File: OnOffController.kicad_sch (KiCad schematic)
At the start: 10 parts, among them J1 USB_B_Micro, U1 STM6601, U2 MCP73831-2-OT, U3 SPX3819M5-L

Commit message: Finished schematic
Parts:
- added C2, C3: 10uF, Capacitor_SMD:C_1206_3216Metric_Pad1.33x1.80mm_HandSolder, symbol Device:C
- added C4, C5: 1uF, Capacitor_SMD:C_1206_3216Metric_Pad1.33x1.80mm_HandSolder, symbol Device:C
- added C6: .33uF, Capacitor_SMD:C_1206_3216Metric_Pad1.33x1.80mm_HandSolder, symbol Device:C
- added C7: .1uF, Capacitor_SMD:C_1206_3216Metric_Pad1.33x1.80mm_HandSolder, symbol Device:C
- added D2: MBR0520, Diode_SMD:D_SOD-123, symbol Diode:MBR0520
- added D3: LED, LED_SMD:LED_1206_3216Metric_Pad1.42x1.75mm_HandSolder, symbol Device:LED
- added J2, J5: Conn_01x02_Pin, symbol Connector:Conn_01x02_Pin
- added J3, J4: Conn_01x04_Pin, symbol Connector:Conn_01x04_Pin
- added J6, J7: Conn_01x03_Pin, symbol Connector:Conn_01x03_Pin
- added R10, R5, R6, R7: 10K, Resistor_SMD:R_1206_3216Metric_Pad1.30x1.75mm_HandSolder, symbol Device:R
- added R8: 3.48K, Resistor_SMD:R_1206_3216Metric_Pad1.30x1.75mm_HandSolder, symbol Device:R
- added R9: 1K, Resistor_SMD:R_1206_3216Metric_Pad1.30x1.75mm_HandSolder, symbol Device:R
- added SW1: 2-1437565-8, 2-1437565-8:SW_SMD_2-1437565-8_4_4.50_6.00_6.00_5.00, symbol 2-1437565-8_CustomSwitch:2-1437565-8
- added TP1, TP2, TP3, TP4, TP5: TestPoint, symbol Connector:TestPoint
- C1: footprint (none) -> Capacitor_SMD:C_1206_3216Metric_Pad1.33x1.80mm_HandSolder
- D1: footprint (none) -> LED_SMD:LED_1206_3216Metric_Pad1.42x1.75mm_HandSolder
- R1, R2, R3, R4: footprint (none) -> Resistor_SMD:R_1206_3216Metric_Pad1.30x1.75mm_HandSolder
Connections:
- net GND: now also U1.12 (GND), U3.2 (GND), C2.2, C3.2, C4.2, C5.2, C6.2, C7.2, J2.2 (Pin_2), J4.4 (Pin_4), J7.1 (Pin_1), J7.2 (Pin_2), J7.3 (Pin_3), R10.2, SW1.1, SW1.2, TP2.1
- net VBUS: now also U1.1 (Vcc), U3.1 (IN), C2.1, C7.1, D2.1 (K), R9.1, TP3.1, TP4.1
- net VDC: now also D2.2 (A), TP5.1
- net EN_DIV: now reaches U3.3 (EN)
- net EN_DIV: now also J3.4 (Pin_4), R10.1, R8.2
- net +3V3: now reaches U3.5 (OUT)
- net +3V3: now also C3.1, C4.1, J3.1 (Pin_1), J5.1 (Pin_1), J6.1 (Pin_1), J6.2 (Pin_2), J6.3 (Pin_3), R5.1, R6.1, R7.1, TP1.1
- net BAT_SENSE: now reaches R3.2, R4.1
- net BAT_SENSE: now also J4.3 (Pin_3)
- net RST: now reaches U1.10 (~{RST})
- net RST: now also J3.3 (Pin_3), R6.2
- net INT: now reaches U1.11 (~{INT})
- net INT: now also J3.2 (Pin_2), R7.2
- net at U1.2 (~{SR}): now also U1.6 (~{PB}), J2.1 (Pin_1), SW1.3, SW1.4
- net Vref: now reaches U1.3 (Vref)
- net Vref: now also C5.1
- net PS_HOLD: now reaches U1.4 (PS_HOLD)
- net PS_HOLD: now also J4.2 (Pin_2), J5.2 (Pin_2)
- net at U1.5 (C_SRD): now also C6.1
- net at U1.7 (~{VCC}_LO): now also D3.1 (K)
- net PB_OUT: now reaches U1.8 (~{PB}_OUT)
- net PB_OUT: now also J4.1 (Pin_1), R5.2
- net EN: now reaches U1.9 (~{EN}/EN)
- net EN: now also R8.1
- new net: D3.2 (A), R9.2
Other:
- moved on the sheet: C1, D1, J1, R1, R2, R3, R4, U1, U2, U3

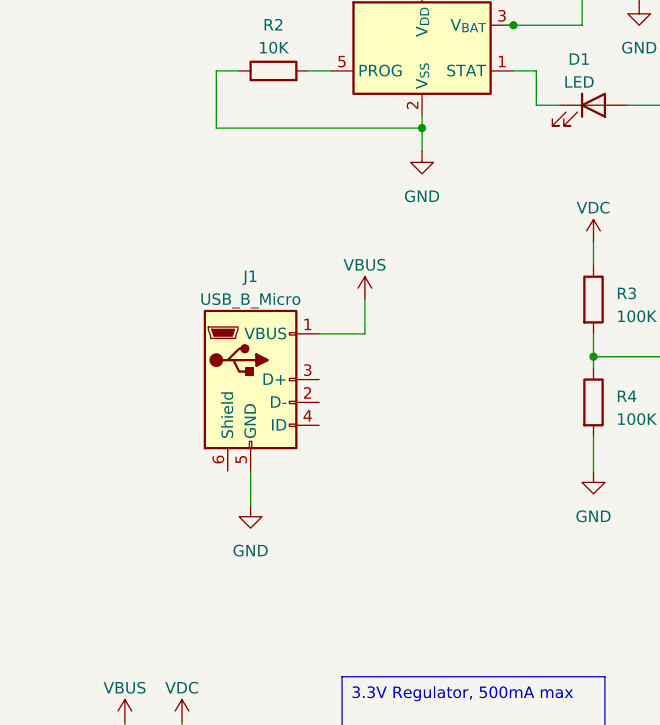
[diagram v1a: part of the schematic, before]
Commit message: Updated USB-B and switch footprints
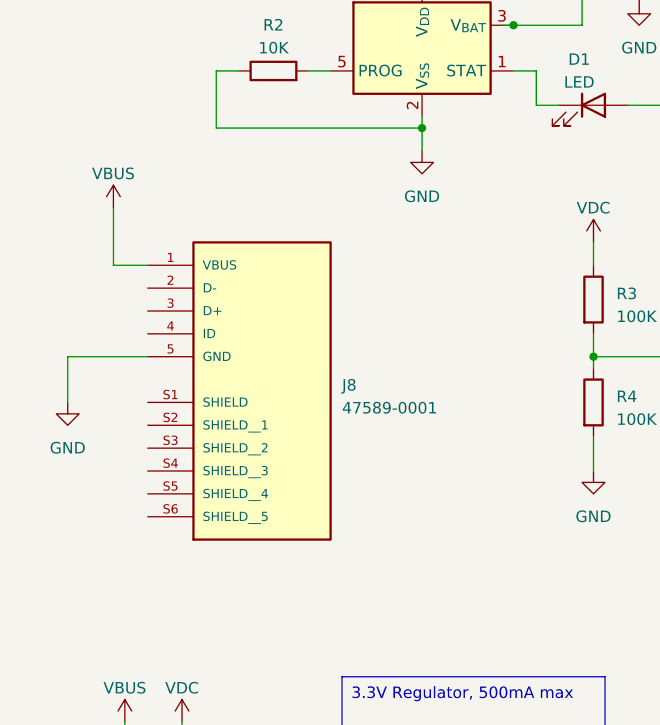
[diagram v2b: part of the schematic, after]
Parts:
- removed J1: USB_B_Micro, symbol Connector:USB_B_Micro
- added J8: 47589-0001, 47589_0001_USB_B:MOLEX_47589-0001, symbol 47589-0001_MOLEX_USB_B:47589-0001
- SW1: footprint 2-1437565-8:SW_SMD_2-1437565-8_4_4.50_6.00_6.00_5.00 -> FSM2JSMAA-2:SW_SMD_2-1437565-8_4_4.50_6.00_6.00_5.00
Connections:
- net GND: now also J8.5 (GND)
- net VBUS: now also J8.1 (VBUS)
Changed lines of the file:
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@@
-    (stroke (width 0) (type default))
-  )
-  (wire (pts (xy 48.26 74.93) (xy 53.34 74.93))
     (stroke (width 0) (type default))
   )
@@
     (stroke (width 0) (type default))
   )
-  (wire (pts (xy 53.34 74.93) (xy 53.34 71.12))
-    (stroke (width 0) (type default))
-  )
   (wire (pts (xy 68.58 40.64) (xy 69.85 40.64))
     (stroke (width 0) (type default))
@@
     (stroke (width 0) (type default))
   )
+  (wire (pts (xy 25.4 67.31) (xy 29.21 67.31))
+    (stroke (width 0) (type default))
+  )
   (wire (pts (xy 207.01 138.43) (xy 207.01 140.97))
     (stroke (width 0) (type default))
@@
     (stroke (width 0) (type default))
   )
+  (wire (pts (xy 29.21 77.47) (xy 20.32 77.47))
+    (stroke (width 0) (type default))
+  )
   (wire (pts (xy 227.33 86.36) (xy 231.14 86.36))
     (stroke (width 0) (type default))
   )
+  (wire (pts (xy 20.32 77.47) (xy 20.32 82.55))
+    (stroke (width 0) (type default))
+  )
   (wire (pts (xy 252.73 33.02) (xy 252.73 29.21))
     (stroke (width 0) (type default))
@@
     (stroke (width 0) (type default))
   )
-  (wire (pts (xy 40.64 90.17) (xy 40.64 93.98))
-    (stroke (width 0) (type default))
-  )
   (wire (pts (xy 69.85 45.72) (xy 72.39 45.72))
     (stroke (width 0) (type default))
@@
   )
   (wire (pts (xy 69.85 40.64) (xy 77.47 40.64))
+    (stroke (width 0) (type default))
+  )
+  (wire (pts (xy 25.4 60.96) (xy 25.4 67.31))
     (stroke (width 0) (type default))
   )
@@
         (path "/7d14c1c9-e9e0-4f5d-aab8-9d06ff75a31a"
           (reference "TP1") (unit 1)
+        )
+      )
+    )
+  )
+  (symbol (lib_id "power:GND") (at 20.32 82.55 0) (unit 1)
+    (in_bom yes) (on_board yes) (dnp no) (fields_autoplaced)
+    (property "Reference" "#PWR034" (at 20.32 88.9 0)
+      (effects (font (size 1.27 1.27)) hide)
+    )
+    (property "Value" "GND" (at 20.32 87.63 0)
+      (effects (font (size 1.27 1.27)))
+    )
+    (property "Footprint" "" (at 20.32 82.55 0)
+      (effects (font (size 1.27 1.27)) hide)
+    )
+    (property "Datasheet" "" (at 20.32 82.55 0)
+      (effects (font (size 1.27 1.27)) hide)
+    )
+    (pin "1")
+    (instances
+      (project "OnOffController"
+        (path "/7d14c1c9-e9e0-4f5d-aab8-9d06ff75a31a"
+          (reference "#PWR034") (unit 1)
         )
       )
@@
     )
   )
-  (symbol (lib_id "power:VBUS") (at 53.34 71.12 0) (unit 1)
-    (in_bom yes) (on_board yes) (dnp no) (fields_autoplaced)
-    (property "Reference" "#PWR08" (at 53.34 74.93 0)
-      (effects (font (size 1.27 1.27)) hide)
-    )
-    (property "Value" "VBUS" (at 53.34 67.31 0)
-      (effects (font (size 1.27 1.27)))
-    )
-    (property "Footprint" "" (at 53.34 71.12 0)
-      (effects (font (size 1.27 1.27)) hide)
-    )
-    (property "Datasheet" "" (at 53.34 71.12 0)
-      (effects (font (size 1.27 1.27)) hide)
-    )
-    (pin "1")
-    (instances
-      (project "OnOffController"
-        (path "/7d14c1c9-e9e0-4f5d-aab8-9d06ff75a31a"
-          (reference "#PWR08") (unit 1)
-        )
-      )
-    )
-  )
   (symbol (lib_id "Device:C") (at 83.82 34.29 0) (unit 1)
     (in_bom yes) (on_board yes) (dnp no) (fields_autoplaced)
@@
     )
   )
+  (symbol (lib_id "power:VBUS") (at 25.4 60.96 0) (unit 1)
+    (in_bom yes) (on_board yes) (dnp no) (fields_autoplaced)
+    (property "Reference" "#PWR033" (at 25.4 64.77 0)
+      (effects (font (size 1.27 1.27)) hide)
+    )
+    (property "Value" "VBUS" (at 25.4 57.15 0)
+      (effects (font (size 1.27 1.27)))
+    )
+    (property "Footprint" "" (at 25.4 60.96 0)
+      (effects (font (size 1.27 1.27)) hide)
+    )
+    (property "Datasheet" "" (at 25.4 60.96 0)
+      (effects (font (size 1.27 1.27)) hide)
+    )
+    (pin "1")
+    (instances
+      (project "OnOffController"
+        (path "/7d14c1c9-e9e0-4f5d-aab8-9d06ff75a31a"
+          (reference "#PWR033") (unit 1)
+        )
+      )
+    )
+  )
   (symbol (lib_id "Device:R") (at 207.01 132.08 0) (unit 1)
     (in_bom yes) (on_board yes) (dnp no) (fields_autoplaced)
@@
       (effects (font (size 1.27 1.27)) (justify right))
     )
-    (property "Footprint" "2-1437565-8:SW_SMD_2-1437565-8_4_4.50_6.00_6.00_5.00" (at 158.75 80.01 0)
+    (property "Footprint" "FSM2JSMAA-2:SW_SMD_2-1437565-8_4_4.50_6.00_6.00_5.00" (at 158.75 80.01 0)
       (effects (font (size 1.27 1.27)) (justify bottom) hide)
     )
@@
     )
   )
-  (symbol (lib_id "power:GND") (at 40.64 93.98 0) (unit 1)
-    (in_bom yes) (on_board yes) (dnp no) (fields_autoplaced)
-    (property "Reference" "#PWR09" (at 40.64 100.33 0)
-      (effects (font (size 1.27 1.27)) hide)
-    )
-    (property "Value" "GND" (at 40.64 99.06 0)
-      (effects (font (size 1.27 1.27)))
-    )
-    (property "Footprint" "" (at 40.64 93.98 0)
-      (effects (font (size 1.27 1.27)) hide)
-    )
-    (property "Datasheet" "" (at 40.64 93.98 0)
-      (effects (font (size 1.27 1.27)) hide)
-    )
-    (pin "1")
-    (instances
-      (project "OnOffController"
-        (path "/7d14c1c9-e9e0-4f5d-aab8-9d06ff75a31a"
-          (reference "#PWR09") (unit 1)
-        )
-      )
-    )
-  )
-  (symbol (lib_id "Device:R") (at 212.09 36.83 0) (unit 1)
-    (in_bom yes) (on_board yes) (dnp no) (fields_autoplaced)
-    (property "Reference" "R7" (at 214.63 36.195 0)
-      (effects (font (size 1.27 1.27)) (justify left))
-    )
-    (property "Value" "10K" (at 214.63 38.735 0)
-      (effects (font (size 1.27 1.27)) (justify left))
-    )
-    (property "Footprint" "Resistor_SMD:R_1206_3216Metric_Pad1.30x1.75mm_HandSolder" (at 210.312 36.83 90)
-      (effects (font (size 1.27 1.27)) hide)
-    )
-    (property "Datasheet" "~" (at 212.09 36.83 0)
-      (effects (font (size 1.27 1.27)) hide)
-    )
-    (pin "1")
-    (pin "2")
-    (instances
-      (project "OnOffController"
-        (path "/7d14c1c9-e9e0-4f5d-aab8-9d06ff75a31a"
-          (reference "R7") (unit 1)
-        )
-      )
-    )
-  )
-  (symbol (lib_id "Connector:USB_B_Micro") (at 40.64 80.01 0) (unit 1)
-    (in_bom yes) (on_board yes) (dnp no) (fields_autoplaced)
-    (property "Reference" "J1" (at 40.64 68.58 0)
-      (effects (font (size 1.27 1.27)))
-    )
-    (property "Value" "USB_B_Micro" (at 40.64 71.12 0)
-      (effects (font (size 1.27 1.27)))
-    )
-    (property "Footprint" "" (at 44.45 81.28 0)
-      (effects (font (size 1.27 1.27)) hide)
-    )
-    (property "Datasheet" "~" (at 44.45 81.28 0)
-      (effects (font (size 1.27 1.27)) hide)
+  (symbol (lib_id "47589-0001_MOLEX_USB_B:47589-0001") (at 41.91 74.93 0) (unit 1)
+    (in_bom yes) (on_board yes) (dnp no) (fields_autoplaced)
+    (property "Reference" "J8" (at 50.8 80.645 0)
+      (effects (font (size 1.27 1.27)) (justify left))
+    )
+    (property "Value" "47589-0001" (at 50.8 83.185 0)
+      (effects (font (size 1.27 1.27)) (justify left))
+    )
+    (property "Footprint" "47589_0001_USB_B:MOLEX_47589-0001" (at 41.91 74.93 0)
+      (effects (font (size 1.27 1.27)) (justify bottom) hide)
+    )
+    (property "Datasheet" "" (at 41.91 74.93 0)
+      (effects (font (size 1.27 1.27)) hide)
+    )
+    (property "PARTREV" "G" (at 41.91 74.93 0)
+      (effects (font (size 1.27 1.27)) (justify bottom) hide)
+    )
+    (property "STANDARD" "Manufacturer Recommendations" (at 41.91 74.93 0)
+      (effects (font (size 1.27 1.27)) (justify bottom) hide)
+    )
+    (property "MAXIMUM_PACKAGE_HEIGHT" "2.65 mm" (at 41.91 74.93 0)
+      (effects (font (size 1.27 1.27)) (justify bottom) hide)
+    )
+    (property "MANUFACTURER" "Molex" (at 41.91 74.93 0)
+      (effects (font (size 1.27 1.27)) (justify bottom) hide)
     )
     (pin "1")
@@
     (pin "4")
     (pin "5")
-    (pin "6")
-    (instances
-      (project "OnOffController"
-        (path "/7d14c1c9-e9e0-4f5d-aab8-9d06ff75a31a"
-          (reference "J1") (unit 1)
-        )
-      )
+    (pin "S1")
+    (pin "S2")
+    (pin "S3")
+    (pin "S4")
+    (pin "S5")
+    (pin "S6")
+    (instances
+      (project "OnOffController"
+        (path "/7d14c1c9-e9e0-4f5d-aab8-9d06ff75a31a"
+          (reference "J8") (unit 1)
+        )
+      )
+    )
+  )
+  (symbol (lib_id "Device:R") (at 212.09 36.83 0) (unit 1)
+    (in_bom yes) (on_board yes) (dnp no) (fields_autoplaced)
+    (property "Reference" "R7" (at 214.63 36.195 0)
+      (effects (font (size 1.27 1.27)) (justify left))
+    )
+    (property "Value" "10K" (at 214.63 38.735 0)
+      (effects (font (size 1.27 1.27)) (justify left))
+    )
+    (property "Footprint" "Resistor_SMD:R_1206_3216Metric_Pad1.30x1.75mm_HandSolder" (at 210.312 36.83 90)
+      (effects (font (size 1.27 1.27)) hide)
+    )
+    (property "Datasheet" "~" (at 212.09 36.83 0)
+      (effects (font (size 1.27 1.27)) hide)
+    )
+    (pin "1")
+    (pin "2")
+    (instances
+      (project "OnOffController"
+        (path "/7d14c1c9-e9e0-4f5d-aab8-9d06ff75a31a"
+          (reference "R7") (unit 1)
+        )
+      )

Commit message: Generated PCB files
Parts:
- removed J5: Conn_01x02_Pin, symbol Connector:Conn_01x02_Pin
- removed J6, J7: Conn_01x03_Pin, symbol Connector:Conn_01x03_Pin
- removed SW1: 2-1437565-8, FSM2JSMAA-2:SW_SMD_2-1437565-8_4_4.50_6.00_6.00_5.00, symbol 2-1437565-8_CustomSwitch:2-1437565-8
- added J1: S2B-PH-K-SLFSN, Connector_JST:JST_PH_S2B-PH-SM4-TB_1x02-1MP_P2.00mm_Horizontal, symbol 2024-04-06_16-40-21_JSTPH:S2B-PH-K-SLFSN
- added JP1: SolderJumper_2_Bridged, Jumper:SolderJumper-2_P1.3mm_Bridged_Pad1.0x1.5mm, symbol Jumper:SolderJumper_2_Bridged
- added SW1: KMR211GLFS, KMR2_Switch:KMR2xxG_CNK, symbol 2024-04-06_17-09-25_KMR_Switch:KMR211GLFS
- C1, C2, C3, C4, C5, C6, C7: footprint Capacitor_SMD:C_1206_3216Metric_Pad1.33x1.80mm_HandSolder -> Capacitor_SMD:C_0603_1608Metric_Pad1.08x0.95mm_HandSolder
- D1: footprint LED_SMD:LED_1206_3216Metric_Pad1.42x1.75mm_HandSolder -> LED_SMD:LED_0805_2012Metric_Pad1.15x1.40mm_HandSolder
- D3: footprint LED_SMD:LED_1206_3216Metric_Pad1.42x1.75mm_HandSolder -> LED_SMD:LED_0603_1608Metric_Pad1.05x0.95mm_HandSolder
- J2: footprint (none) -> Connector_PinHeader_2.54mm:PinHeader_1x02_P2.54mm_Vertical
- J3, J4: footprint (none) -> Connector_PinHeader_2.54mm:PinHeader_1x04_P2.54mm_Vertical
- R1, R10, R2, R3, R4, R5, R6, R7, R8, R9: footprint Resistor_SMD:R_1206_3216Metric_Pad1.30x1.75mm_HandSolder -> Resistor_SMD:R_0603_1608Metric_Pad0.98x0.95mm_HandSolder
- TP1, TP2, TP3, TP4, TP5: footprint (none) -> TestPoint:TestPoint_Pad_D1.5mm
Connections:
- net +3V3: now also JP1.2 (B)
- net GND: now also J1.2, SW1.1, SW1.3
- net PS_HOLD: now also JP1.1 (A)
- net VDC: now also J1.1
- net at J2.1 (Pin_1), U1.2 (~{SR}), U1.6 (~{PB}): now also SW1.2, SW1.4
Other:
- moved on the sheet: C2, C3, C4, D2, J8, R3, R4, R5, R6, R7, TP1, TP2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

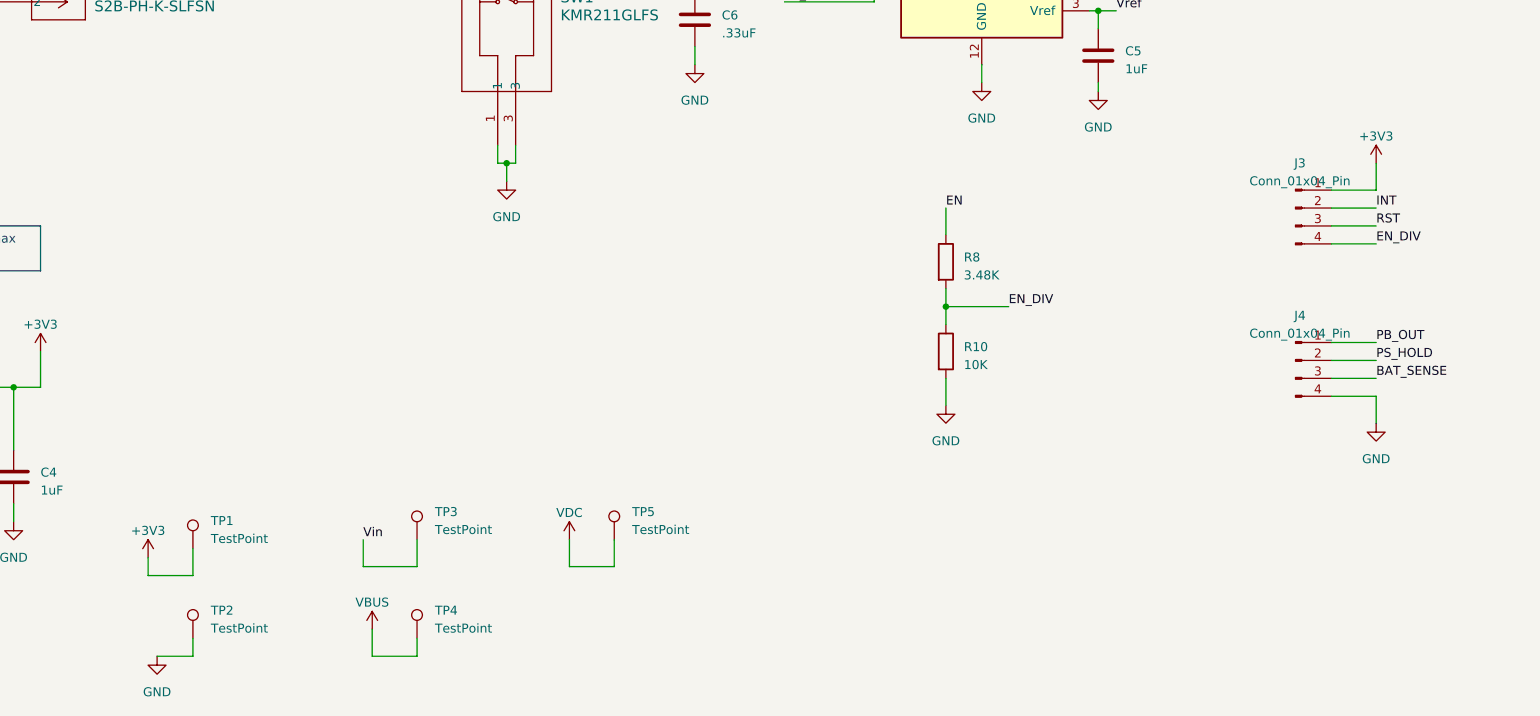
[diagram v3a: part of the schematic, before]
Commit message: Passing DRC and added all silk screens
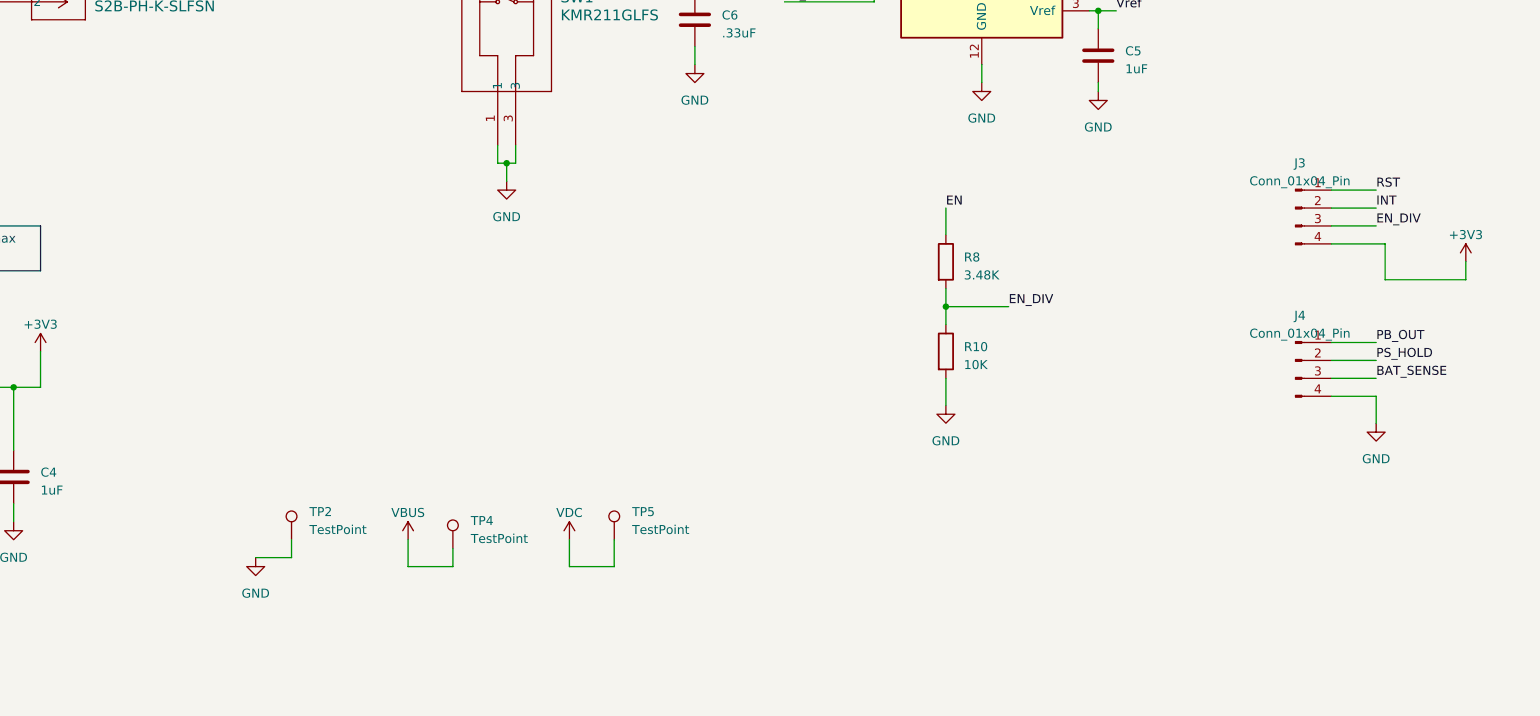
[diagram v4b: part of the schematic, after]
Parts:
- removed TP1, TP3: TestPoint, TestPoint:TestPoint_Pad_D1.5mm, symbol Connector:TestPoint
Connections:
- net +3V3: now also J3.4 (Pin_4); no longer J3.1 (Pin_1)
- net EN_DIV: now also J3.3 (Pin_3); no longer J3.4 (Pin_4)
- net RST: now also J3.1 (Pin_1); no longer J3.3 (Pin_3)
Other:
- moved on the sheet: TP2, TP4

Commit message: Added BOM
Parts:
- R8: value 3.48K -> 2.5K
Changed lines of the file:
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@@
       (effects (font (size 1.27 1.27)) (justify left))
     )
-    (property "Value" "3.48K" (at 209.55 133.985 0)
+    (property "Value" "2.5K" (at 209.55 133.985 0)
       (effects (font (size 1.27 1.27)) (justify left))
     )
